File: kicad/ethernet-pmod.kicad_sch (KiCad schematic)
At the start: 26 parts, among them J1 PMOD, J2 RJ45_AMP_RJMG1, J3 MDIO, U1 LAN8720A

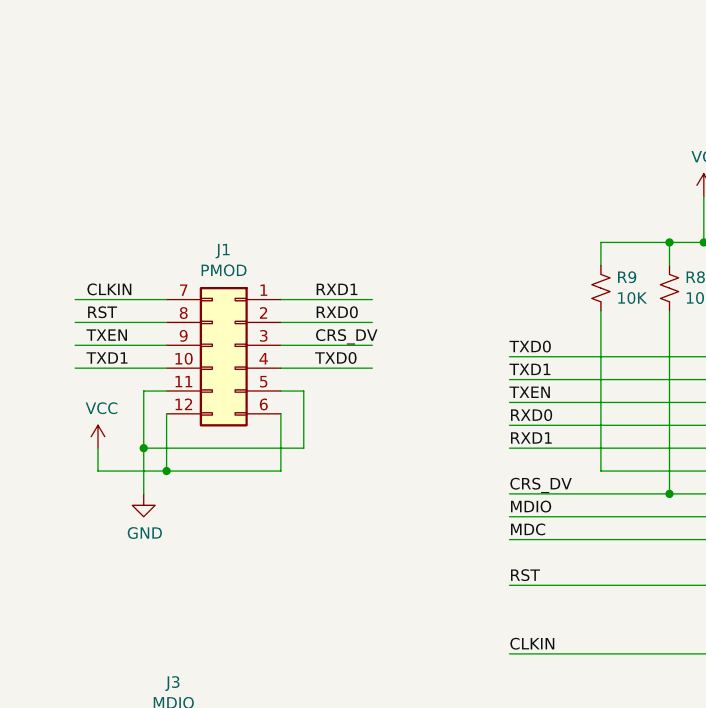
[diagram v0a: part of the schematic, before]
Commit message: cleanup: improve PMOD header (J1) presentation in schematic
- tidied up schematic
- added commentary on pin orientation
- renamed RST to RSTn for clarity
- re-exported schematic to PDF
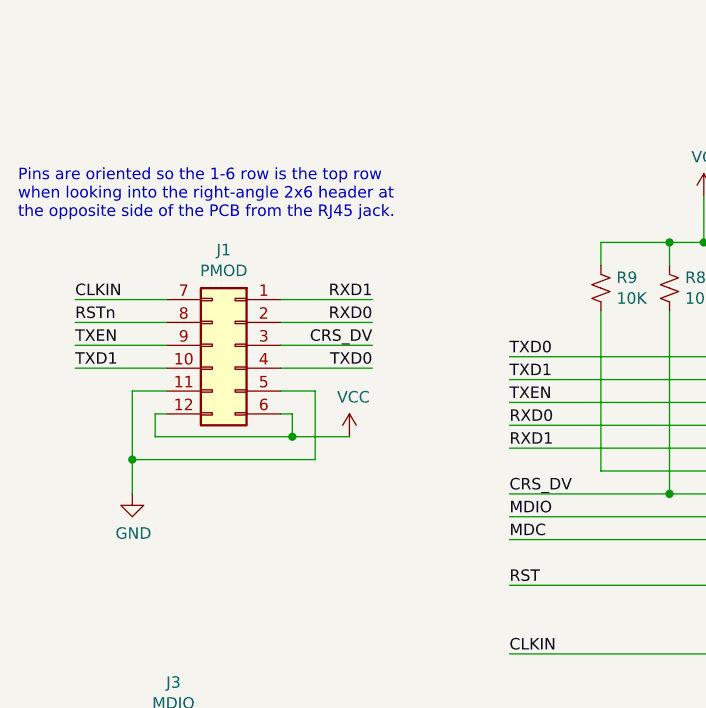
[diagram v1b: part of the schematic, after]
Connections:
- net RST: no longer J1.8 (Pin_8)
- new net RSTn: J1.8 (Pin_8)
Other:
- note added: "Pins are oriented so the 1-6 row is the top row when looking into the right-angle 2x6 header at the opposite side of the PCB from the RJ45 jack."
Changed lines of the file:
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@@
   (junction (at 184.15 60.96) (diameter 0) (color 0 0 0 0)
   )
+  (junction (at 52.07 88.9) (diameter 0) (color 0 0 0 0)
+  )
   (junction (at 176.53 85.09) (diameter 0) (color 0 0 0 0)
   )
@@
   (junction (at 207.01 90.17) (diameter 0) (color 0 0 0 0)
   )
-  (junction (at 35.56 90.17) (diameter 0) (color 0 0 0 0)
-  )
   (junction (at 93.98 67.31) (diameter 0) (color 0 0 0 0)
   )
   (junction (at 168.91 82.55) (diameter 0) (color 0 0 0 0)
   )
+  (junction (at 34.29 91.44) (diameter 0) (color 0 0 0 0)
+  )
   (junction (at 128.27 36.83) (diameter 0) (color 0 0 0 0)
   )
@@
   )
   (junction (at 101.6 67.31) (diameter 0) (color 0 0 0 0)
-  )
-  (junction (at 38.1 92.71) (diameter 0) (color 0 0 0 0)
   )
   (junction (at 101.6 90.17) (diameter 0) (color 0 0 0 0)
@@
     (stroke (width 0) (type default) (color 0 0 0 0))
   )
+  (wire (pts (xy 36.83 86.36) (xy 38.1 86.36))
+    (stroke (width 0) (type default) (color 0 0 0 0))
+  )
   (wire (pts (xy 119.38 43.18) (xy 119.38 44.45))
     (stroke (width 0) (type default) (color 0 0 0 0))
@@
     (stroke (width 0) (type default) (color 0 0 0 0))
   )
-  (wire (pts (xy 30.48 92.71) (xy 30.48 90.17))
-    (stroke (width 0) (type default) (color 0 0 0 0))
-  )
   (wire (pts (xy 187.96 100.33) (xy 210.82 100.33))
     (stroke (width 0) (type default) (color 0 0 0 0))
@@
     (stroke (width 0) (type default) (color 0 0 0 0))
   )
-  (wire (pts (xy 35.56 90.17) (xy 53.34 90.17))
-    (stroke (width 0) (type default) (color 0 0 0 0))
-  )
-  (wire (pts (xy 35.56 90.17) (xy 35.56 95.25))
-    (stroke (width 0) (type default) (color 0 0 0 0))
-  )
-  (wire (pts (xy 38.1 92.71) (xy 50.8 92.71))
-    (stroke (width 0) (type default) (color 0 0 0 0))
-  )
   (wire (pts (xy 119.38 55.88) (xy 119.38 53.34))
     (stroke (width 0) (type default) (color 0 0 0 0))
@@
     (stroke (width 0) (type default) (color 0 0 0 0))
   )
+  (wire (pts (xy 34.29 91.44) (xy 34.29 95.25))
+    (stroke (width 0) (type default) (color 0 0 0 0))
+  )
   (wire (pts (xy 207.01 60.96) (xy 207.01 82.55))
     (stroke (width 0) (type default) (color 0 0 0 0))
   )
-  (wire (pts (xy 38.1 86.36) (xy 38.1 92.71))
-    (stroke (width 0) (type default) (color 0 0 0 0))
-  )
   (wire (pts (xy 168.91 82.55) (xy 160.02 82.55))
     (stroke (width 0) (type default) (color 0 0 0 0))
   )
+  (wire (pts (xy 52.07 86.36) (xy 52.07 88.9))
+    (stroke (width 0) (type default) (color 0 0 0 0))
+  )
   (wire (pts (xy 207.01 90.17) (xy 210.82 90.17))
     (stroke (width 0) (type default) (color 0 0 0 0))
   )
-  (wire (pts (xy 38.1 92.71) (xy 30.48 92.71))
+  (wire (pts (xy 34.29 91.44) (xy 54.61 91.44))
     (stroke (width 0) (type default) (color 0 0 0 0))
   )
@@
     (stroke (width 0) (type default) (color 0 0 0 0))
   )
+  (wire (pts (xy 36.83 88.9) (xy 36.83 86.36))
+    (stroke (width 0) (type default) (color 0 0 0 0))
+  )
   (wire (pts (xy 151.13 38.1) (xy 151.13 36.83))
     (stroke (width 0) (type default) (color 0 0 0 0))
   )
+  (wire (pts (xy 52.07 88.9) (xy 58.42 88.9))
+    (stroke (width 0) (type default) (color 0 0 0 0))
+  )
   (wire (pts (xy 121.92 95.25) (xy 93.98 95.25))
     (stroke (width 0) (type default) (color 0 0 0 0))
@@
     (stroke (width 0) (type default) (color 0 0 0 0))
   )
+  (wire (pts (xy 36.83 88.9) (xy 52.07 88.9))
+    (stroke (width 0) (type default) (color 0 0 0 0))
+  )
   (wire (pts (xy 203.2 82.55) (xy 203.2 80.01))
     (stroke (width 0) (type default) (color 0 0 0 0))
@@
     (stroke (width 0) (type default) (color 0 0 0 0))
   )
-  (wire (pts (xy 50.8 92.71) (xy 50.8 86.36))
-    (stroke (width 0) (type default) (color 0 0 0 0))
-  )
   (polyline (pts (xy 200.66 68.58) (xy 204.47 68.58))
     (stroke (width 0) (type default) (color 0 0 0 0))
@@
     (stroke (width 0) (type default) (color 0 0 0 0))
   )
-  (wire (pts (xy 53.34 83.82) (xy 50.8 83.82))
+  (wire (pts (xy 54.61 83.82) (xy 50.8 83.82))
     (stroke (width 0) (type default) (color 0 0 0 0))
   )
@@
     (stroke (width 0) (type default) (color 0 0 0 0))
   )
-  (wire (pts (xy 53.34 90.17) (xy 53.34 83.82))
+  (wire (pts (xy 54.61 91.44) (xy 54.61 83.82))
     (stroke (width 0) (type default) (color 0 0 0 0))
   )
@@
     (stroke (width 0) (type default) (color 0 0 0 0))
   )
+  (wire (pts (xy 50.8 86.36) (xy 52.07 86.36))
+    (stroke (width 0) (type default) (color 0 0 0 0))
+  )
   (wire (pts (xy 41.91 124.46) (xy 50.8 124.46))
     (stroke (width 0) (type default) (color 0 0 0 0))
   )
-  (wire (pts (xy 35.56 83.82) (xy 35.56 90.17))
+  (wire (pts (xy 34.29 83.82) (xy 34.29 91.44))
     (stroke (width 0) (type default) (color 0 0 0 0))
   )
@@
     (stroke (width 0) (type default) (color 0 0 0 0))
   )
-  (wire (pts (xy 38.1 83.82) (xy 35.56 83.82))
+  (wire (pts (xy 38.1 83.82) (xy 34.29 83.82))
     (stroke (width 0) (type default) (color 0 0 0 0))
   )
@@
     (effects (font (size 1.27 1.27)) (justify left bottom))
   )
+  (text "Pins are oriented so the 1-6 row is the top row\nwhen looking into the right-angle 2x6 header at\nthe opposite side of the PCB from the RJ45 jack."
+    (at 21.59 64.77 0)
+    (effects (font (size 1.27 1.27)) (justify left bottom))
+  )
   (text "MODE=111 (Autonegotiate)" (at 93.98 132.08 0)
     (effects (font (size 1.27 1.27)) (justify left bottom))
@@
     (effects (font (size 1.27 1.27)) (justify left bottom))
   )
-  (label "CRS_DV" (at 54.61 78.74 0)
-    (effects (font (size 1.27 1.27)) (justify left bottom))
+  (label "CRS_DV" (at 60.96 78.74 180)
+    (effects (font (size 1.27 1.27)) (justify right bottom))
   )
   (label "RBIAS" (at 161.29 97.79 0)
@@
     (effects (font (size 1.27 1.27)) (justify left bottom))
   )
-  (label "CLKIN" (at 29.21 73.66 0)
+  (label "CLKIN" (at 27.94 73.66 0)
     (effects (font (size 1.27 1.27)) (justify left bottom))
   )
@@
     (effects (font (size 1.27 1.27)) (justify left bottom))
   )
-  (label "RXD0" (at 54.61 76.2 0)
-    (effects (font (size 1.27 1.27)) (justify left bottom))
-  )
-  (label "TXEN" (at 29.21 78.74 0)
+  (label "RXD0" (at 60.96 76.2 180)
+    (effects (font (size 1.27 1.27)) (justify right bottom))
+  )
+  (label "TXEN" (at 27.94 78.74 0)
     (effects (font (size 1.27 1.27)) (justify left bottom))
   )
@@
     (effects (font (size 1.27 1.27)) (justify left bottom))
   )
-  (label "TXD0" (at 54.61 81.28 0)
-    (effects (font (size 1.27 1.27)) (justify left bottom))
+  (label "TXD0" (at 60.96 81.28 180)
+    (effects (font (size 1.27 1.27)) (justify right bottom))
   )
   (label "TXEN" (at 76.2 85.09 0)
@@
     (effects (font (size 1.27 1.27)) (justify left bottom))
   )
-  (label "TXD1" (at 29.21 81.28 0)
+  (label "TXD1" (at 27.94 81.28 0)
     (effects (font (size 1.27 1.27)) (justify left bottom))
   )
@@
     (effects (font (size 1.27 1.27)) (justify left bottom))
   )
-  (label "RST" (at 29.21 76.2 0)
-    (effects (font (size 1.27 1.27)) (justify left bottom))
-  )
-  (label "RXD1" (at 54.61 73.66 0)
-    (effects (font (size 1.27 1.27)) (justify left bottom))
+  (label "RSTn" (at 27.94 76.2 0)
+    (effects (font (size 1.27 1.27)) (justify left bottom))
+  )
+  (label "RXD1" (at 60.96 73.66 180)
+    (effects (font (size 1.27 1.27)) (justify right bottom))
   )
   (label "TXN" (at 161.29 85.09 0)
@@
     (pin "1")
   )
-  (symbol (lib_id "power:VCC") (at 30.48 90.17 0) (unit 1)
-    (in_bom yes) (on_board yes)
-    (property "Reference" "#PWR0112" (id 0) (at 30.48 93.98 0)
-      (effects (font (size 1.27 1.27)) hide)
-    )
-    (property "Value" "VCC" (id 1) (at 30.9118 85.7758 0))
-    (property "Footprint" "" (id 2) (at 30.48 90.17 0)
-      (effects (font (size 1.27 1.27)) hide)
-    )
-    (property "Datasheet" "" (id 3) (at 30.48 90.17 0)
-      (effects (font (size 1.27 1.27)) hide)
-    )
-    (pin "1")
-  )
-  (symbol (lib_id "power:GND") (at 35.56 95.25 0) (unit 1)
-    (in_bom yes) (on_board yes)
-    (property "Reference" "#PWR0113" (id 0) (at 35.56 101.6 0)
-      (effects (font (size 1.27 1.27)) hide)
-    )
-    (property "Value" "GND" (id 1) (at 35.687 99.6442 0))
-    (property "Footprint" "" (id 2) (at 35.56 95.25 0)
-      (effects (font (size 1.27 1.27)) hide)
-    )
-    (property "Datasheet" "" (id 3) (at 35.56 95.25 0)
-      (effects (font (size 1.27 1.27)) hide)
-    )
+  (symbol (lib_id "power:VCC") (at 58.42 88.9 0) (unit 1)
+    (in_bom yes) (on_board yes)
+    (property "Reference" "#PWR0112" (id 0) (at 58.42 92.71 0)
+      (effects (font (size 1.27 1.27)) hide)
+    )
+    (property "Value" "VCC" (id 1) (at 58.8518 84.5058 0))
+    (property "Footprint" "" (id 2) (at 58.42 88.9 0)
+      (effects (font (size 1.27 1.27)) hide)
+    )
+    (property "Datasheet" "" (id 3) (at 58.42 88.9 0)
+      (effects (font (size 1.27 1.27)) hide)
+    )
+    (pin "1")
+  )
+  (symbol (lib_id "power:GND") (at 34.29 95.25 0) (unit 1)
+    (in_bom yes) (on_board yes)
+    (property "Reference" "#PWR0113" (id 0) (at 34.29 101.6 0)
+      (effects (font (size 1.27 1.27)) hide)
+    )
+    (property "Value" "GND" (id 1) (at 34.417 99.6442 0))
+    (property "Footprint" "" (id 2) (at 34.29 95.25 0)
+      (effects (font (size 1.27 1.27)) hide)
+    )
+    (property "Datasheet" "" (id 3) (at 34.29 95.25 0)
+      (effects (font (size 1.27 1.27)) hide)
+    )
